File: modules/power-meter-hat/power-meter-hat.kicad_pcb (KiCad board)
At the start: 2 copper layers, 65 x 56 mm, 50 parts, among them J1 Barrel_Jack_Switch, J2 GPIO, J3 OutputTerminal, J5 OutputTerminal, J7 OutputTerminal, Q1 BC856BDW1, Q2 SI2301CDS, U1 CAT24C256, U2 NCP1117-3.3_SOT223, U3 INA219AxD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

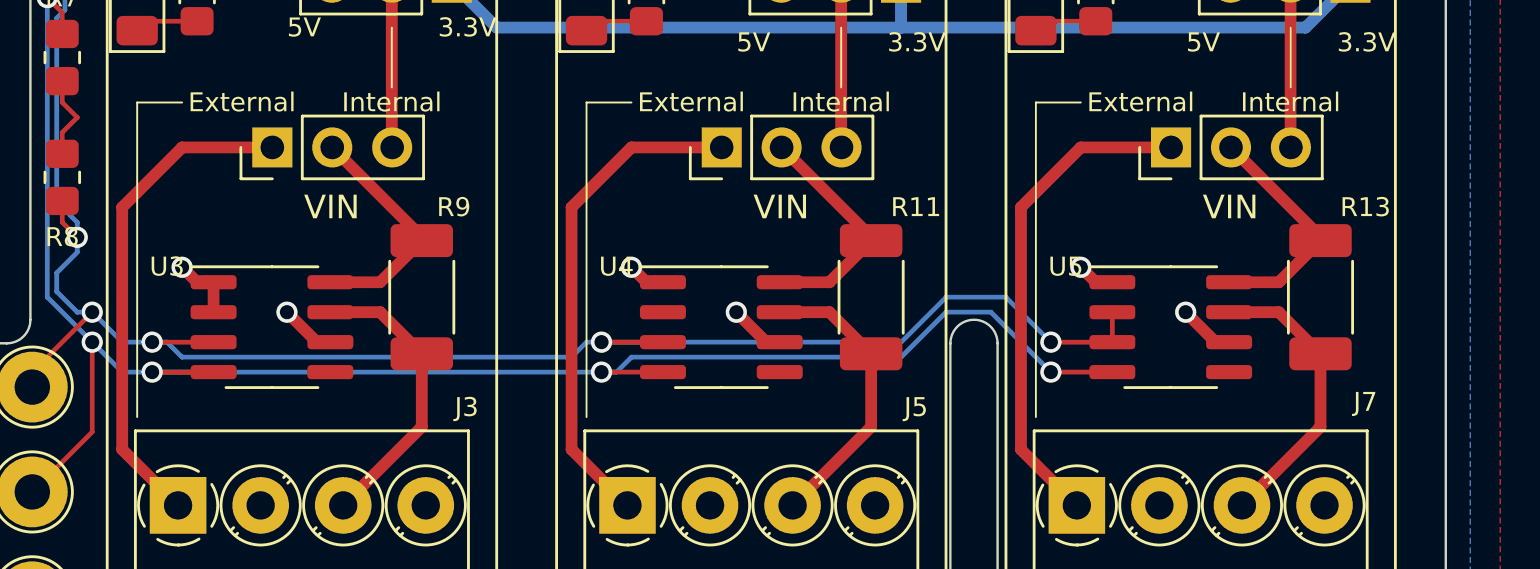
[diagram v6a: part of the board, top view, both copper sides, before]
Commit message: Add bypass capacitors for INA219
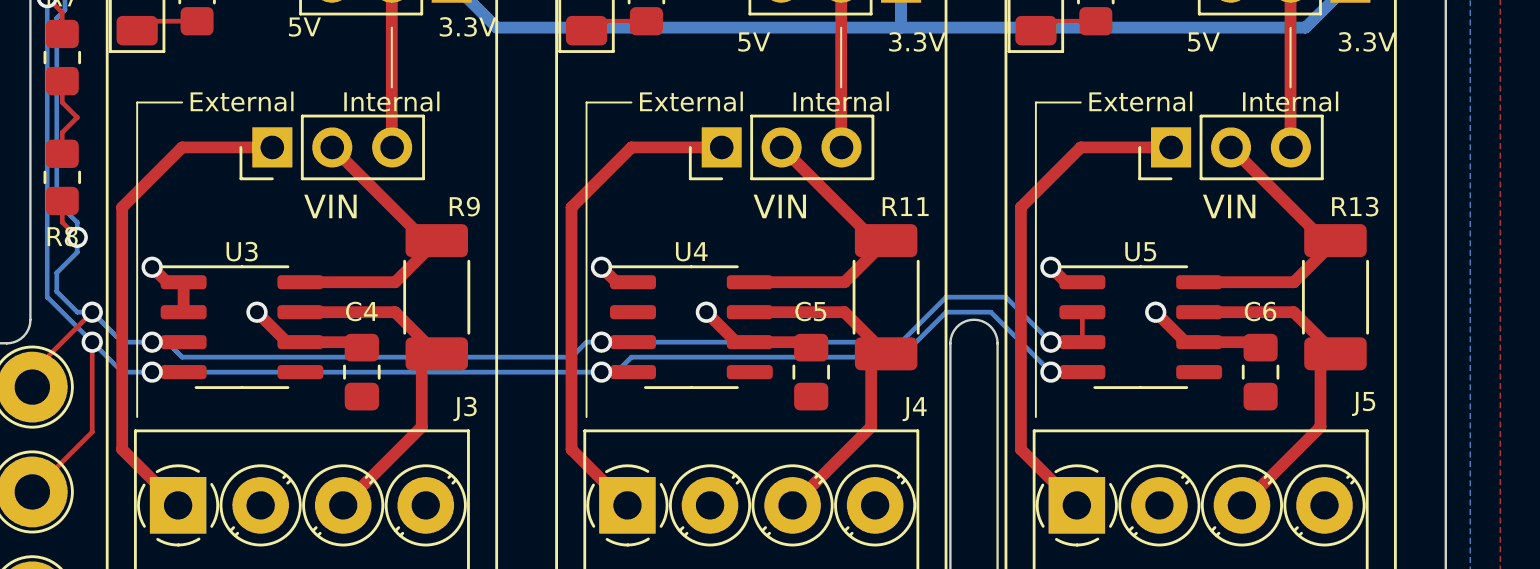
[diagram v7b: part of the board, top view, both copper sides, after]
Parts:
- added C4: C, Capacitor_SMD:C_0805_2012Metric_Pad1.18x1.45mm_HandSolder, F.Cu at (119.0, 82.2)
- added C5: C, Capacitor_SMD:C_0805_2012Metric_Pad1.18x1.45mm_HandSolder, F.Cu at (138.1, 82.2)
- added C6: C, Capacitor_SMD:C_0805_2012Metric_Pad1.18x1.45mm_HandSolder, F.Cu at (157.2, 82.2)
- moved U5 1.27 mm to (152.1, 80.3)
- moved U3 1.27 mm to (114.0, 80.3)
- moved U4 1.27 mm to (133.0, 80.3)
- moved R11 0.64 mm to (141.3, 79.0)
- moved R13 0.63 mm to (160.3, 79.0)
- moved R9 0.63 mm to (122.2, 79.0)
- renumbered J5 to J4, J7 to J5, JP2 to JP1, JP1 to JP2
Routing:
- net GND: track 32.7 -> 40.8 mm
- net /SCL: track 103.4 -> 98.3 mm
- net /SDA: track 95.5 -> 90.4 mm
- net /PowerChannel 1/VIN: track 9.97 -> 12.6 mm
- net /PowerChannel 1/VOUT: track 12.4 -> 14.3 mm
- net /PowerChannel 3/VOUT: track 12.4 -> 14.3 mm
- net /PowerChannel 3/VIN: track 9.97 -> 11.9 mm
- net /PowerChannel 2/VIN: track 9.97 -> 11.9 mm
- net /PowerChannel 2/VOUT: track 12.4 -> 14.3 mm
